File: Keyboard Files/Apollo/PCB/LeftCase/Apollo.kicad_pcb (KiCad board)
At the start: 2 copper layers, 151.9 x 125.5 mm, 93 parts, among them J1 AVR-ISP-6, SW1 SW_Push, U1 PRTR5V0U2X, U2 ATmega32U4-MU, Y1 Crystal_GND24_Small

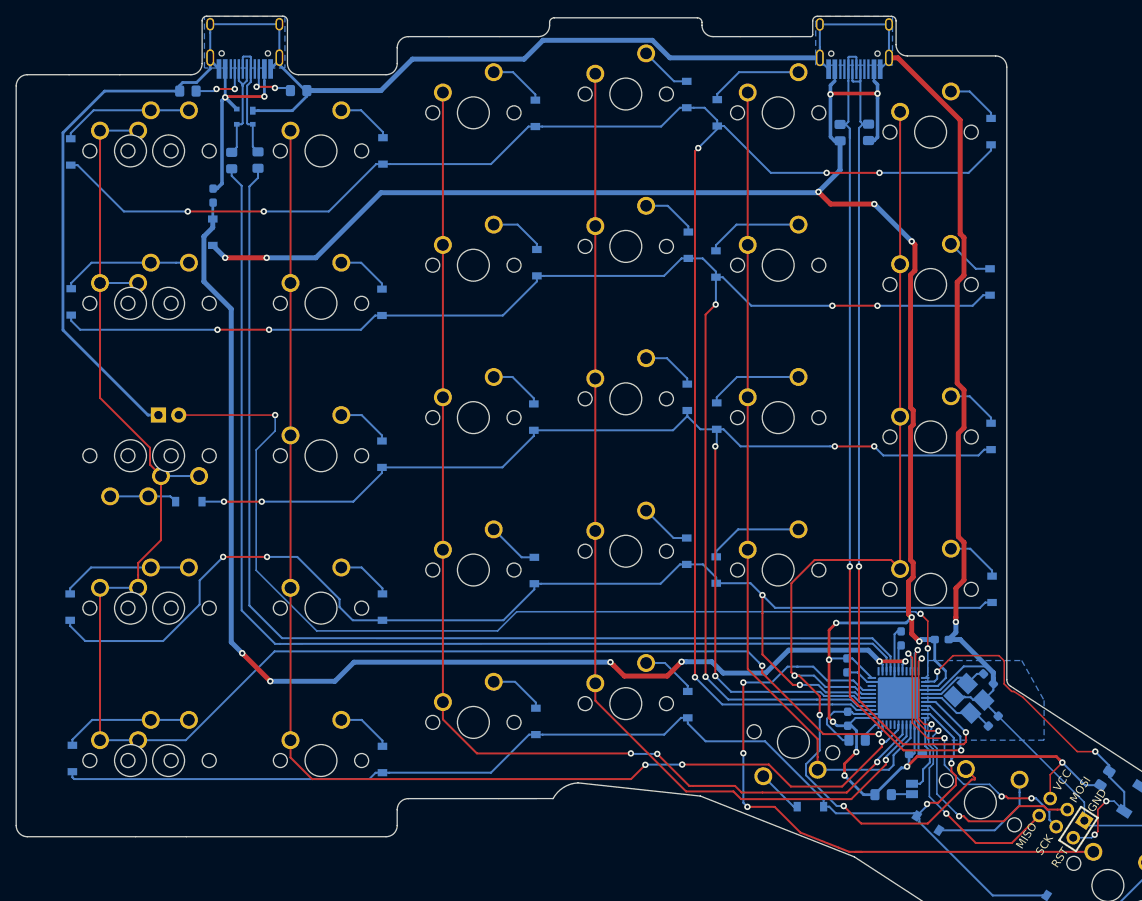
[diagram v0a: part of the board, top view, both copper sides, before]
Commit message: Update Apollo plates, export pcb and plate svgs
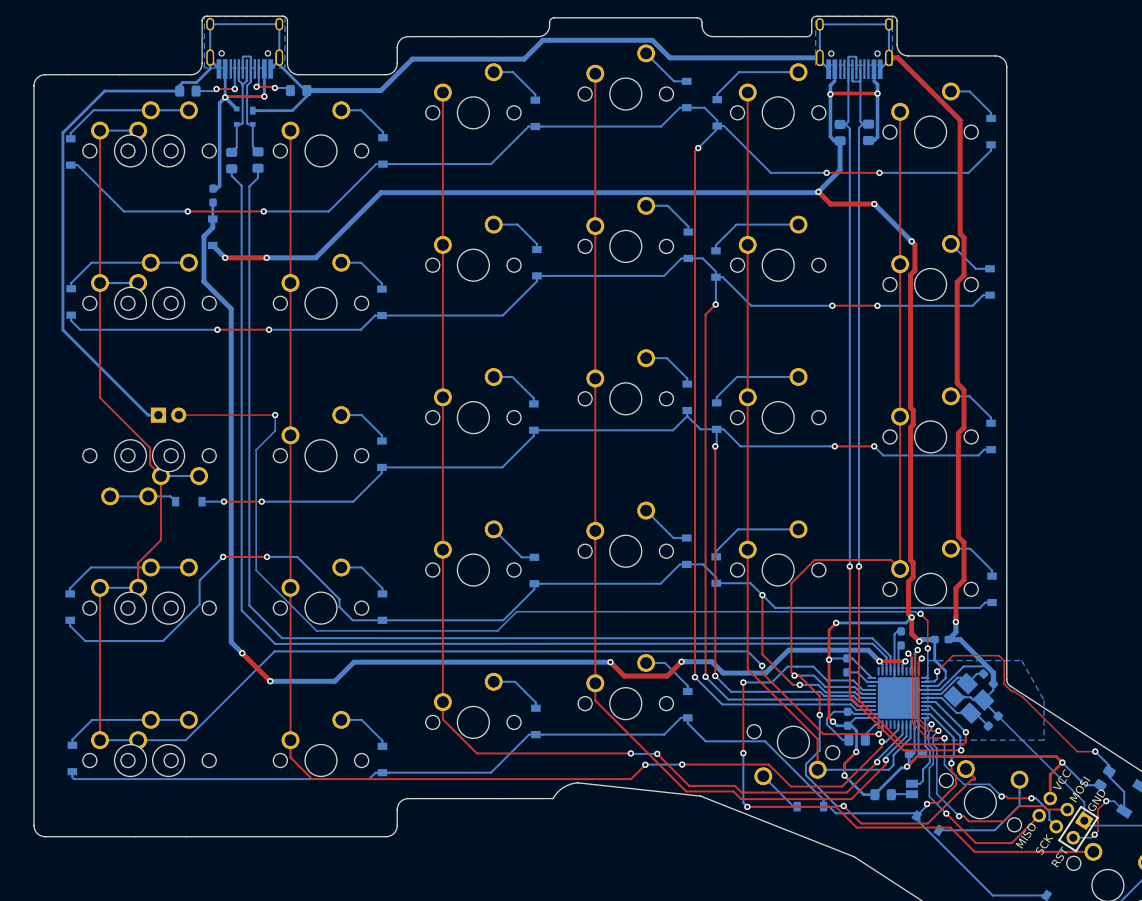
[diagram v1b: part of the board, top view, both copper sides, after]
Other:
- board size 151.9 x 125.5 mm -> 149.7 x 125.5 mm

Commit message: Increase Apollo plate bezel
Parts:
- added C10: 0.1uF, Capacitor_SMD:C_0603_1608Metric_Pad1.05x0.95mm_HandSolder, B.Cu at (253.6, 149.5)
- added C11: 10uF, Capacitor_SMD:C_0603_1608Metric_Pad1.05x0.95mm_HandSolder, B.Cu at (265.8, 147.1)
- added C12: 22pF, Capacitor_SMD:C_0603_1608Metric_Pad1.05x0.95mm_HandSolder, B.Cu at (247.5, 141.0)
- added C13: 22pF, Capacitor_SMD:C_0603_1608Metric_Pad1.05x0.95mm_HandSolder, B.Cu at (247.8, 146.2)
- added C14: 1uF, Capacitor_SMD:C_0603_1608Metric_Pad1.05x0.95mm_HandSolder, B.Cu at (260.3, 151.7)
- added C8: 0.1uF, Capacitor_SMD:C_0603_1608Metric_Pad1.05x0.95mm_HandSolder, B.Cu at (266.1, 140.6)
- added C9: 0.1uF, Capacitor_SMD:C_0603_1608Metric_Pad1.05x0.95mm_HandSolder, B.Cu at (258.4, 137.1)
- added D33: D_Small, Diode_SMD:D_SOD-123, B.Cu at (247.0, 73.5)
- added D34: D_Small, Diode_SMD:D_SOD-123, B.Cu at (281.4, 71.0)
- added D35: D_Small, Diode_SMD:D_SOD-123, B.Cu at (300.4, 68.6)
- added D36: D_Small, Diode_SMD:D_SOD-123, B.Cu at (319.6, 70.7)
- added D37: D_Small, Diode_SMD:D_SOD-123, B.Cu at (323.0, 75.6)
- added D38: D_Small, Diode_SMD:D_SOD-123, B.Cu at (362.7, 75.6)
- added D39: D_Small, Diode_SMD:D_SOD-123, B.Cu at (247.0, 92.2)
- added D40: D_Small, Diode_SMD:D_SOD-123, B.Cu at (281.4, 89.8)
- added D41: D_Small, Diode_SMD:D_SOD-123, B.Cu at (300.4, 87.5)
- added D42: D_Small, Diode_SMD:D_SOD-123, B.Cu at (319.5, 89.7)
- added D43: D_Small, Diode_SMD:D_SOD-123, B.Cu at (323.1, 94.4)
- added D44: D_Small, Diode_SMD:D_SOD-123, B.Cu at (362.8, 94.7)
- added D45: Schottky, Diode_SMD:D_SOD-123, B.Cu at (335.0, 84.9)
- added D46: D_Small, Diode_SMD:D_SOD-123, B.Cu at (246.8, 111.4)
- added D47: D_Small, Diode_SMD:D_SOD-123, B.Cu at (281.2, 108.9)
- added D48: D_Small, Diode_SMD:D_SOD-123, B.Cu at (300.4, 106.5)
- added D49: D_Small, Diode_SMD:D_SOD-123, B.Cu at (319.5, 108.8)
- added D50: D_Small, Diode_SMD:D_SOD-123, B.Cu at (323.0, 113.6)
- added D51: D_Small, Diode_SMD:D_SOD-123, B.Cu at (362.7, 114.0)
- added D52: D_Small, Diode_SMD:D_SOD-123, B.Cu at (246.9, 130.6)
- added D53: D_Small, Diode_SMD:D_SOD-123, B.Cu at (281.4, 128.3)
- added D54: D_Small, Diode_SMD:D_SOD-123, B.Cu at (300.5, 125.7)
- added D55: D_Small, Diode_SMD:D_SOD-123, B.Cu at (319.5, 128.1)
- added D56: D_Small, Diode_SMD:D_SOD-123, B.Cu at (322.8, 131.6)
- added D57: D_Small, Diode_SMD:D_SOD-123, B.Cu at (362.7, 132.8)
- added D58: D_Small, Diode_SMD:D_SOD-123, B.Cu at (238.8, 169.7)
- added D59: D_Small, Diode_SMD:D_SOD-123, B.Cu at (254.9, 159.5)
- added D60: D_Small, Diode_SMD:D_SOD-123, B.Cu at (284.9, 153.6)
- added D61: D_Small, Diode_SMD:D_SOD-123, B.Cu at (300.4, 144.8)
- added D62: D_Small, Diode_SMD:D_SOD-123, B.Cu at (319.5, 147.2)
- added D63: D_Small, Diode_SMD:D_SOD-123, B.Cu at (322.8, 151.9)
- added D64: D_Small, Diode_SMD:D_SOD-123, B.Cu at (363.0, 151.8)
- added F2: 500mA, Fuse:Fuse_0603_1608Metric_Pad1.05x0.95mm_HandSolder, B.Cu at (336.7, 80.9)
- added J10: Conn_01x01, locallib:breakaway-mousebites, F.Cu at (122.9, 161.4)
- added J11: Conn_01x01, locallib:breakaway-mousebites, F.Cu at (358.3, 66.2)
- added J12: Conn_01x01, locallib:breakaway-mousebites, F.Cu at (350.8, 161.4)
- added J13: Conn_01x01, locallib:breakaway-mousebites, F.Cu at (305.3, 161.4)
- added J14: Conn_01x01, locallib:breakaway-mousebites, F.Cu at (305.3, 156.7)
- added J15: Conn_01x01, locallib:breakaway-mousebites, F.Cu at (69.2, 61.4)
- added J16: Conn_01x01, locallib:breakaway-mousebites, F.Cu at (358.3, 61.4)
- added J17: Conn_01x01, Connector_PinHeader_2.54mm:PinHeader_1x01_P2.54mm_Vertical, F.Cu at (180.9, 123.5)
- added J2: AVR-ISP-6, Molex-0548190589:Reset_Pretty-Mask, F.Cu at (237.5, 158.6)
- added J3: Conn_01x01, locallib:breakaway-mousebites, F.Cu at (69.2, 66.2)
- added J4: Conn_01x01, locallib:breakaway-mousebites, F.Cu at (116.6, 61.4)
- added J5: Conn_01x01, locallib:breakaway-mousebites, F.Cu at (311.1, 61.4)
- added J6: Conn_01x01, locallib:breakaway-mousebites, F.Cu at (153.0, 61.4)
- added J7: Conn_01x01, locallib:breakaway-mousebites, F.Cu at (275.8, 61.4)
- added J8: Conn_01x01, locallib:breakaway-mousebites, F.Cu at (77.5, 161.4)
- added J9: Conn_01x01, locallib:breakaway-mousebites, F.Cu at (122.9, 156.7)
- added JP2: Jumper_NO, Jumper:SolderJumper-2_P1.3mm_Open_Pad1.0x1.5mm, B.Cu at (252.6, 136.5)
- added MX32: MX-NoLED, MX_Only:MXOnly-1U-NoLED, F.Cu at (254.5, 73.3)
- added MX33: MX-NoLED, MX_Only:MXOnly-1U-NoLED, F.Cu at (273.6, 70.9)
- added MX34: MX-NoLED, MX_Only:MXOnly-1U-NoLED, F.Cu at (292.6, 68.6)
- added MX35: MX-NoLED, MX_Only:MXOnly-1U-NoLED, F.Cu at (311.7, 70.9)
- added MX36: MX-NoLED, MX_Only:MXOnly-1U-NoLED, F.Cu at (330.7, 75.7)
- added MX37: MX-NoLED, MX_Only:MXOnly-1.5U-NoLED, F.Cu at (354.5, 75.7)
- added MX38: MX-NoLED, MX_Only:MXOnly-1U-NoLED, F.Cu at (254.5, 92.4)
- added MX39: MX-NoLED, MX_Only:MXOnly-1U-NoLED, F.Cu at (273.6, 90.0)
- added MX40: MX-NoLED, MX_Only:MXOnly-1U-NoLED, F.Cu at (292.6, 87.6)
- added MX41: MX-NoLED, MX_Only:MXOnly-1U-NoLED, F.Cu at (311.7, 90.0)
- added MX42: MX-NoLED, MX_Only:MXOnly-1U-NoLED, F.Cu at (330.7, 94.7)
- added MX43: MX-NoLED, MX_Only:MXOnly-1.5U-NoLED, F.Cu at (354.5, 94.7)
- added MX44: MX-NoLED, MX_Only:MXOnly-1U-NoLED, F.Cu at (254.5, 111.4)
- added MX45: MX-NoLED, MX_Only:MXOnly-1U-NoLED, F.Cu at (273.6, 109.0)
- added MX46: MX-NoLED, MX_Only:MXOnly-1U-NoLED, F.Cu at (292.6, 106.7)
- added MX47: MX-NoLED, MX_Only:MXOnly-1U-NoLED, F.Cu at (311.7, 109.0)
- added MX48: MX-NoLED, MX_Only:MXOnly-1U-NoLED, F.Cu at (330.7, 113.8)
- added MX49: MX-NoLED, MX_Only:MXOnly-1.5U-NoLED, F.Cu at (354.5, 113.8)
- added MX50: MX-NoLED, MX_Only:MXOnly-1U-NoLED, F.Cu at (254.5, 130.5)
- added MX51: MX-NoLED, MX_Only:MXOnly-1U-NoLED, F.Cu at (273.6, 128.1)
- added MX52: MX-NoLED, MX_Only:MXOnly-1U-NoLED, F.Cu at (292.6, 125.7)
- added MX53: MX-NoLED, MX_Only:MXOnly-1U-NoLED, F.Cu at (311.7, 128.1)
- added MX54: MX-NoLED, MX_Only:MXOnly-1U-NoLED, F.Cu at (330.7, 132.8)
- added MX55: MX-NoLED, MX_Only:MXOnly-1.5U-NoLED, F.Cu at (354.5, 132.8)
- added MX56: MX-NoLED, MX_Only:MXOnly-1.5U-Vertical-NoLED, F.Cu at (232.3, 167.5)
- added MX57: MX-NoLED, MX_Only:MXOnly-1.5U-Vertical-NoLED, F.Cu at (248.3, 157.2)
- added MX58: MX-NoLED, MX_Only:MXOnly-1U-NoLED, F.Cu at (271.7, 149.6)
- added MX59: MX-NoLED, MX_Only:MXOnly-1U-NoLED, F.Cu at (292.6, 144.8)
- added MX60: MX-NoLED, MX_Only:MXOnly-1U-NoLED, F.Cu at (311.7, 147.1)
- added MX61: MX-NoLED, MX_Only:MXOnly-1U-NoLED, F.Cu at (330.7, 151.9)
- added MX62: MX-NoLED, MX_Only:MXOnly-1.5U-NoLED, F.Cu at (354.5, 151.9)
- added MX68: MX-NoLED, MX_Only:MXOnly-1U-NoLED, F.Cu at (349.8, 75.7)
- added MX69: MX-NoLED, MX_Only:MXOnly-1U-NoLED, F.Cu at (349.8, 94.7)
- added MX70: MX-NoLED, MX_Only:MXOnly-1U-NoLED, F.Cu at (349.8, 113.8)
- added MX71: MX-NoLED, MX_Only:MXOnly-1U-NoLED, F.Cu at (349.8, 132.8)
- added MX72: MX-NoLED, MX_Only:MXOnly-1U-NoLED, F.Cu at (349.8, 151.9)
- added R10: 10k, Resistor_SMD:R_0805_2012Metric_Pad1.15x1.40mm_HandSolder, B.Cu at (250.0, 136.4)
- added R11: 10k, Resistor_SMD:R_0805_2012Metric_Pad1.15x1.40mm_HandSolder, B.Cu at (233.3, 154.6)
- added R12: 22, Resistor_SMD:R_0805_2012Metric_Pad1.15x1.40mm_HandSolder, B.Cu at (341.9, 76.1)
- added R13: 22, Resistor_SMD:R_0805_2012Metric_Pad1.15x1.40mm_HandSolder, B.Cu at (338.6, 76.1)
- added R14: 5.1k, Resistor_SMD:R_0805_2012Metric_Pad1.15x1.40mm_HandSolder, B.Cu at (348.3, 67.9)
- added R15: 5.1k, Resistor_SMD:R_0805_2012Metric_Pad1.15x1.40mm_HandSolder, B.Cu at (332.5, 67.9)
- added R16: 10k, Resistor_SMD:R_0805_2012Metric_Pad1.15x1.40mm_HandSolder, B.Cu at (262.8, 134.1)
- added SW2: SW_Push, locallib:SKQGADE010, B.Cu at (227.1, 158.4)
- added U3: PRTR5V0U2X, locallib:SOT143B, B.Cu at (340.2, 71.2)
- added U4: ATmega32U4-MU, Package_DFN_QFN:QFN-44-1EP_7x7mm_P0.5mm_EP5.2x5.2mm, B.Cu at (259.8, 143.7)
- added USB3: HRO-TYPE-C-31-M-12, Type-C:HRO-TYPE-C-31-M-12-HandSoldering, B.Cu at (340.2, 57.3)
- added USB4: HRO-TYPE-C-31-M-12, Type-C:HRO-TYPE-C-31-M-12-HandSoldering, B.Cu at (264.0, 57.3)
- added Y2: Crystal_GND24_Small, Crystal:Crystal_SMD_3225-4Pin_3.2x2.5mm_HandSoldering, B.Cu at (250.6, 143.6)
- moved SW1 46.9 mm to (176.3, 118.9), turned to 0 degrees
- moved R2 43.9 mm to (169.2, 119.0), turned to 90 degrees
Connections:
- J1 pad 5: RST -> Net-(J1-Pad5)
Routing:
- net GNDA: track 0.00 -> 308.1 mm, vias 0 -> 4
- net +5VA: track 0.00 -> 264.5 mm, vias 0 -> 9
- net Col6_1: track 0.00 -> 198.4 mm, vias 0 -> 2
- net Row0_1: track 0.00 -> 197.7 mm, vias 0 -> 6
- net Row1_1: track 0.00 -> 172.4 mm, vias 0 -> 5
- net Row2_1: track 0.00 -> 158.2 mm, vias 0 -> 4
- net VPP: track 0.00 -> 146.7 mm, vias 0 -> 5
- net Col5_1: track 0.00 -> 145.4 mm, vias 0 -> 1
- net Row4_1: track 0.00 -> 145.3 mm, vias 0 -> 2
- net D1_+: track 0.00 -> 145.1 mm
- net D1_-: track 0.00 -> 143.6 mm
- net Row3_1: track 0.00 -> 134.8 mm, vias 0 -> 5
- net Col4_1: track 0.00 -> 128.4 mm, vias 0 -> 1
- net Col3_1: track 0.00 -> 104.7 mm, vias 0 -> 2
- net Col1_1: track 0.00 -> 99.3 mm, vias 0 -> 1
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- added copper zone on B.Cu, net GNDA
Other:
- board size 149.7 x 125.5 mm -> 309.8 x 159.1 mm
